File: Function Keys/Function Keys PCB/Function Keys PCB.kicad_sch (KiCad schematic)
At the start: 0 parts

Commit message: Added keys to schematic
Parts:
- added D? (x13): D_Small, symbol Device:D_Small
- added MX? (x13): MX-NoLED, symbol MX_Alps_Hybrid:MX-NoLED
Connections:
- new net: D?.2 (A), MX?.2 (ROW) (x13)
- new net COL0: MX?.1 (COL)
- new net COL1: MX?.1 (COL)
- new net COL10: MX?.1 (COL)
- new net COL11: MX?.1 (COL)
- new net COL12: MX?.1 (COL)
- new net COL2: MX?.1 (COL)
- new net COL3: MX?.1 (COL)
- new net COL4: MX?.1 (COL)
- new net COL5: MX?.1 (COL)
- new net COL6: MX?.1 (COL)
- new net COL7: MX?.1 (COL)
- new net COL8: MX?.1 (COL)
- new net COL9: MX?.1 (COL)
- new net ROW0: D?.1 (K), D?.1 (K), D?.1 (K), D?.1 (K), D?.1 (K), D?.1 (K), D?.1 (K), D?.1 (K), D?.1 (K), D?.1 (K), D?.1 (K), D?.1 (K), D?.1 (K)

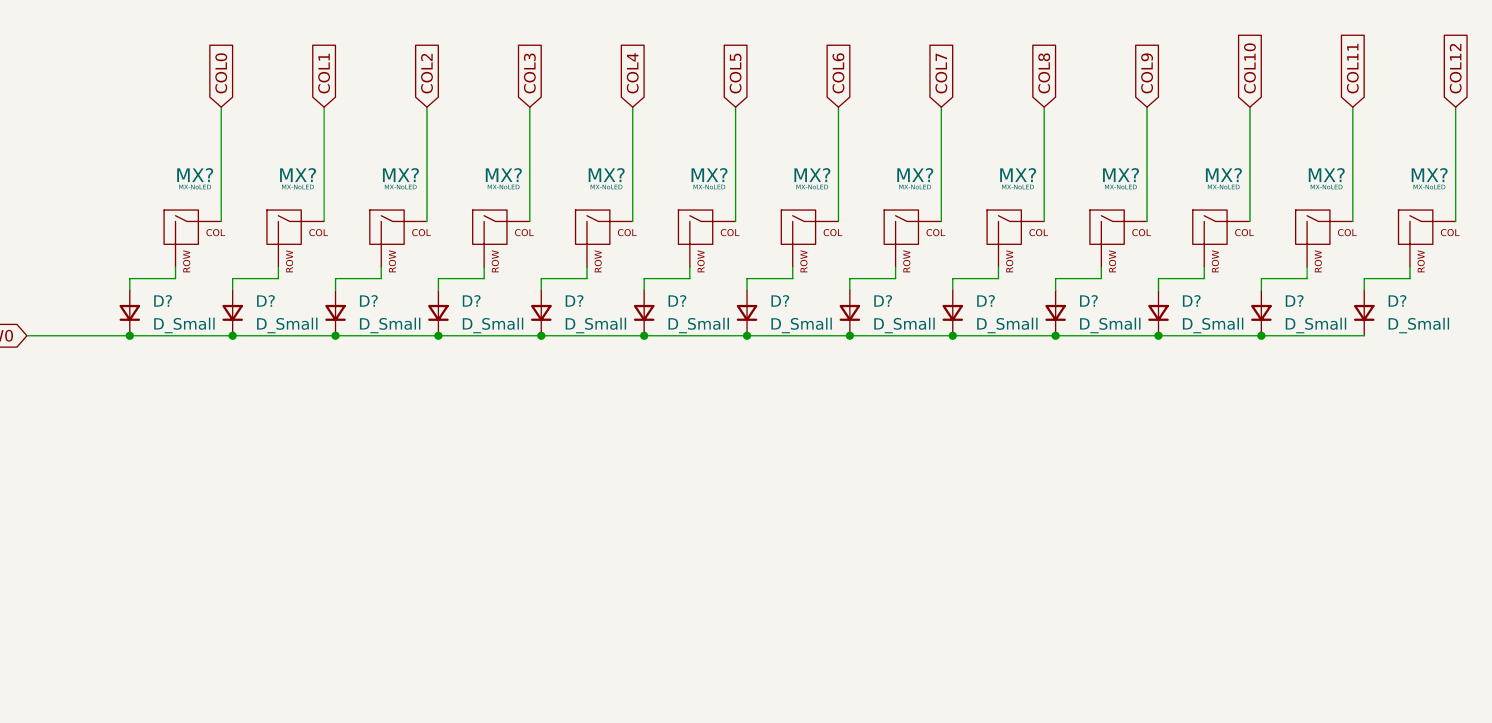
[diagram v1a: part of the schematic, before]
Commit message: Added connectors, labeled keys
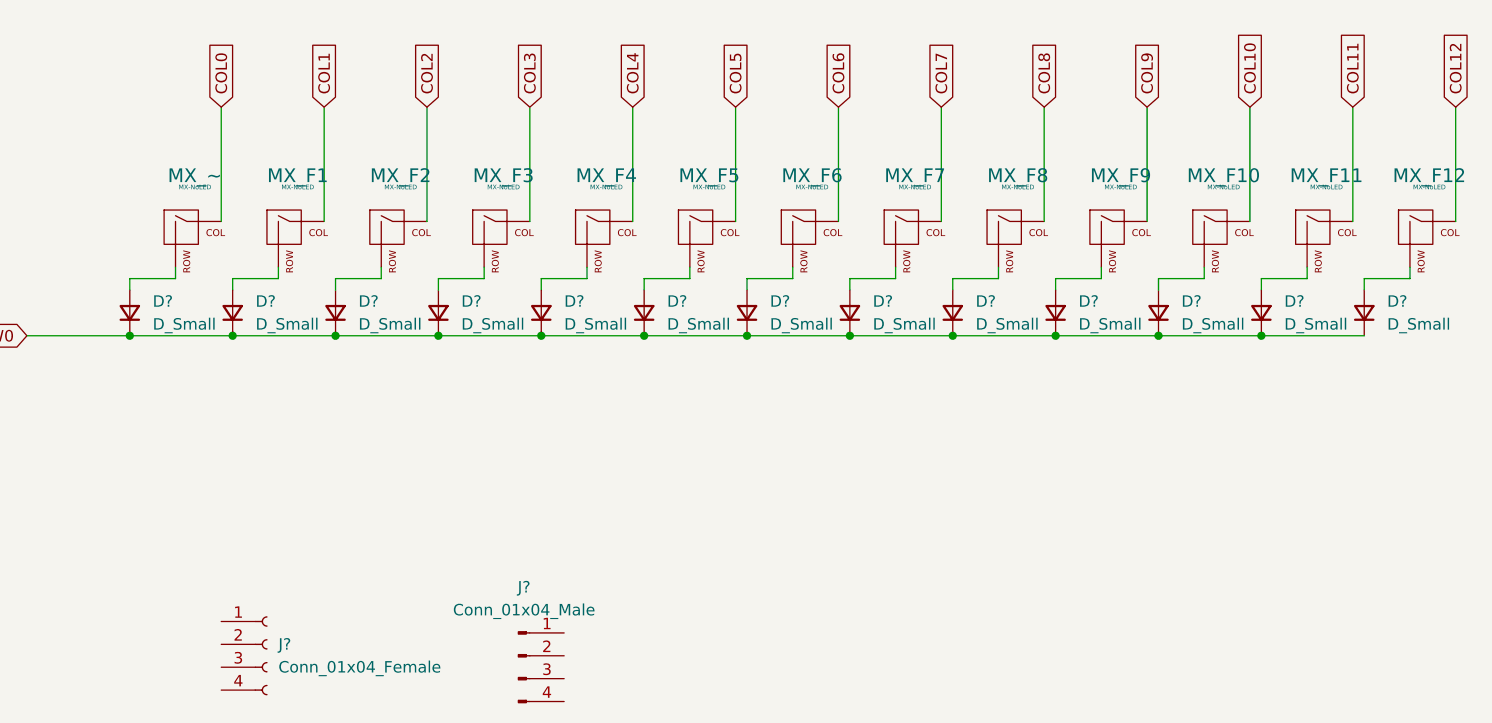
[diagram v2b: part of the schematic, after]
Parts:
- added J?: Conn_01x04_Male, symbol Connector:Conn_01x04_Male
- added J?: Conn_01x04_Female, symbol Connector:Conn_01x04_Female
- gave numbers to parts that had none: 13
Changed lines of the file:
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@@
   (symbol (lib_id "MX_Alps_Hybrid:MX-NoLED") (at 182.88 68.58 0) (unit 1)
     (in_bom yes) (on_board yes) (fields_autoplaced)
-    (property "Reference" "MX?" (id 0) (at 183.7656 62.23 0)
+    (property "Reference" "MX_F8" (id 0) (at 183.7656 62.23 0)
       (effects (font (size 1.524 1.524)))
     )
@@
   (symbol (lib_id "MX_Alps_Hybrid:MX-NoLED") (at 91.44 68.58 0) (unit 1)
     (in_bom yes) (on_board yes) (fields_autoplaced)
-    (property "Reference" "MX?" (id 0) (at 92.3256 62.23 0)
+    (property "Reference" "MX_~" (id 0) (at 92.3256 62.23 0)
       (effects (font (size 1.524 1.524)))
     )
@@
     (pin "2")
   )
+  (symbol (lib_id "Connector:Conn_01x04_Male") (at 128.27 115.57 0) (unit 1)
+    (in_bom yes) (on_board yes) (fields_autoplaced)
+    (property "Reference" "J?" (id 0) (at 128.905 107.95 0))
+    (property "Value" "Conn_01x04_Male" (id 1) (at 128.905 110.49 0))
+    (property "Footprint" "" (id 2) (at 128.27 115.57 0)
+      (effects (font (size 1.27 1.27)) hide)
+    )
+    (property "Datasheet" "~" (id 3) (at 128.27 115.57 0)
+      (effects (font (size 1.27 1.27)) hide)
+    )
+    (pin "1")
+    (pin "2")
+    (pin "3")
+    (pin "4")
+  )
+  (symbol (lib_id "Connector:Conn_01x04_Female") (at 100.33 114.3 0) (unit 1)
+    (in_bom yes) (on_board yes) (fields_autoplaced)
+    (property "Reference" "J?" (id 0) (at 101.6 114.2999 0)
+      (effects (font (size 1.27 1.27)) (justify left))
+    )
+    (property "Value" "Conn_01x04_Female" (id 1) (at 101.6 116.8399 0)
+      (effects (font (size 1.27 1.27)) (justify left))
+    )
+    (property "Footprint" "" (id 2) (at 100.33 114.3 0)
+      (effects (font (size 1.27 1.27)) hide)
+    )
+    (property "Datasheet" "~" (id 3) (at 100.33 114.3 0)
+      (effects (font (size 1.27 1.27)) hide)
+    )
+    (pin "1")
+    (pin "2")
+    (pin "3")
+    (pin "4")
+  )
   (symbol (lib_id "Device:D_Small") (at 222.25 77.47 90) (unit 1)
     (in_bom yes) (on_board yes) (fields_autoplaced)
@@
   (symbol (lib_id "MX_Alps_Hybrid:MX-NoLED") (at 160.02 68.58 0) (unit 1)
     (in_bom yes) (on_board yes) (fields_autoplaced)
-    (property "Reference" "MX?" (id 0) (at 160.9056 62.23 0)
+    (property "Reference" "MX_F6" (id 0) (at 160.9056 62.23 0)
       (effects (font (size 1.524 1.524)))
     )
@@
   (symbol (lib_id "MX_Alps_Hybrid:MX-NoLED") (at 205.74 68.58 0) (unit 1)
     (in_bom yes) (on_board yes) (fields_autoplaced)
-    (property "Reference" "MX?" (id 0) (at 206.6256 62.23 0)
+    (property "Reference" "MX_F10" (id 0) (at 206.6256 62.23 0)
       (effects (font (size 1.524 1.524)))
     )
@@
   (symbol (lib_id "MX_Alps_Hybrid:MX-NoLED") (at 148.59 68.58 0) (unit 1)
     (in_bom yes) (on_board yes) (fields_autoplaced)
-    (property "Reference" "MX?" (id 0) (at 149.4756 62.23 0)
+    (property "Reference" "MX_F5" (id 0) (at 149.4756 62.23 0)
       (effects (font (size 1.524 1.524)))
     )
@@
   (symbol (lib_id "MX_Alps_Hybrid:MX-NoLED") (at 114.3 68.58 0) (unit 1)
     (in_bom yes) (on_board yes) (fields_autoplaced)
-    (property "Reference" "MX?" (id 0) (at 115.1856 62.23 0)
+    (property "Reference" "MX_F2" (id 0) (at 115.1856 62.23 0)
       (effects (font (size 1.524 1.524)))
     )
@@
   (symbol (lib_id "MX_Alps_Hybrid:MX-NoLED") (at 194.31 68.58 0) (unit 1)
     (in_bom yes) (on_board yes) (fields_autoplaced)
-    (property "Reference" "MX?" (id 0) (at 195.1956 62.23 0)
+    (property "Reference" "MX_F9" (id 0) (at 195.1956 62.23 0)
       (effects (font (size 1.524 1.524)))
     )
@@
   (symbol (lib_id "MX_Alps_Hybrid:MX-NoLED") (at 171.45 68.58 0) (unit 1)
     (in_bom yes) (on_board yes) (fields_autoplaced)
-    (property "Reference" "MX?" (id 0) (at 172.3356 62.23 0)
+    (property "Reference" "MX_F7" (id 0) (at 172.3356 62.23 0)
       (effects (font (size 1.524 1.524)))
     )
@@
   (symbol (lib_id "MX_Alps_Hybrid:MX-NoLED") (at 125.73 68.58 0) (unit 1)
     (in_bom yes) (on_board yes) (fields_autoplaced)
-    (property "Reference" "MX?" (id 0) (at 126.6156 62.23 0)
+    (property "Reference" "MX_F3" (id 0) (at 126.6156 62.23 0)
       (effects (font (size 1.524 1.524)))
     )
@@
   (symbol (lib_id "MX_Alps_Hybrid:MX-NoLED") (at 217.17 68.58 0) (unit 1)
     (in_bom yes) (on_board yes) (fields_autoplaced)
-    (property "Reference" "MX?" (id 0) (at 218.0556 62.23 0)
+    (property "Reference" "MX_F11" (id 0) (at 218.0556 62.23 0)
       (effects (font (size 1.524 1.524)))
     )
@@
   (symbol (lib_id "MX_Alps_Hybrid:MX-NoLED") (at 102.87 68.58 0) (unit 1)
     (in_bom yes) (on_board yes) (fields_autoplaced)
-    (property "Reference" "MX?" (id 0) (at 103.7556 62.23 0)
+    (property "Reference" "MX_F1" (id 0) (at 103.7556 62.23 0)
       (effects (font (size 1.524 1.524)))
     )
@@
   (symbol (lib_id "MX_Alps_Hybrid:MX-NoLED") (at 228.6 68.58 0) (unit 1)
     (in_bom yes) (on_board yes) (fields_autoplaced)
-    (property "Reference" "MX?" (id 0) (at 229.4856 62.23 0)
+    (property "Reference" "MX_F12" (id 0) (at 229.4856 62.23 0)
       (effects (font (size 1.524 1.524)))
     )
@@
   (symbol (lib_id "MX_Alps_Hybrid:MX-NoLED") (at 137.16 68.58 0) (unit 1)
     (in_bom yes) (on_board yes) (fields_autoplaced)
-    (property "Reference" "MX?" (id 0) (at 138.0456 62.23 0)
+    (property "Reference" "MX_F4" (id 0) (at 138.0456 62.23 0)
       (effects (font (size 1.524 1.524)))
     )
@@
       (reference "D?") (unit 1) (value "D_Small") (footprint "")
     )
+    (path "/2bb70fb0-16f1-48a5-892c-a37f5f86e428"
+      (reference "J?") (unit 1) (value "Conn_01x04_Male") (footprint "")
+    )
+    (path "/2c079cf8-314d-4fe0-9a70-5d3272650d73"
+      (reference "J?") (unit 1) (value "Conn_01x04_Female") (footprint "")
+    )
+    (path "/953e6a73-9071-4c3b-9621-8aa02821bfc7"
+      (reference "MX_F1") (unit 1) (value "MX-NoLED") (footprint "")
+    )
+    (path "/5d46faef-5a1d-4fde-b7e9-a76b95fc2fec"
+      (reference "MX_F2") (unit 1) (value "MX-NoLED") (footprint "")
+    )
+    (path "/6e281010-a709-474f-8a51-f08f7114458d"
+      (reference "MX_F3") (unit 1) (value "MX-NoLED") (footprint "")
+    )
+    (path "/9dd67abb-a1b2-404e-9cf6-cff85d0f81d3"
+      (reference "MX_F4") (unit 1) (value "MX-NoLED") (footprint "")
+    )
+    (path "/50312df6-7b26-4b0a-afa6-b0ec2230735c"
+      (reference "MX_F5") (unit 1) (value "MX-NoLED") (footprint "")
+    )
+    (path "/433704dd-7939-4149-8b2e-1fb8d447ee43"
+      (reference "MX_F6") (unit 1) (value "MX-NoLED") (footprint "")
+    )
+    (path "/6d341050-f1dc-48f1-9b8d-80e5be0e410d"
+      (reference "MX_F7") (unit 1) (value "MX-NoLED") (footprint "")
+    )
     (path "/004b74d2-af25-4a97-8987-6d8a328283e3"
-      (reference "MX?") (unit 1) (value "MX-NoLED") (footprint "")
+      (reference "MX_F8") (unit 1) (value "MX-NoLED") (footprint "")
+    )
+    (path "/5ddcb211-f334-4231-9e36-52ad5d4d795f"
+      (reference "MX_F9") (unit 1) (value "MX-NoLED") (footprint "")
+    )
+    (path "/4e99f445-0400-4a6f-bb9d-def844852a81"
+      (reference "MX_F10") (unit 1) (value "MX-NoLED") (footprint "")
+    )
+    (path "/93413e48-12b3-4c2b-a7e0-d0a6fc3c6de6"
+      (reference "MX_F11") (unit 1) (value "MX-NoLED") (footprint "")
+    )
+    (path "/9733483c-3919-4675-b73d-10e31040629d"
+      (reference "MX_F12") (unit 1) (value "MX-NoLED") (footprint "")
     )
     (path "/027fa4f5-4265-4496-a2d3-69414343d100"
-      (reference "MX?") (unit 1) (value "MX-NoLED") (footprint "")
-    )
-    (path "/433704dd-7939-4149-8b2e-1fb8d447ee43"
-      (reference "MX?") (unit 1) (value "MX-NoLED") (footprint "")
-    )
-    (path "/4e99f445-0400-4a6f-bb9d-def844852a81"
-      (reference "MX?") (unit 1) (value "MX-NoLED") (footprint "")
-    )
-    (path "/50312df6-7b26-4b0a-afa6-b0ec2230735c"
-      (reference "MX?") (unit 1) (value "MX-NoLED") (footprint "")
-    )
-    (path "/5d46faef-5a1d-4fde-b7e9-a76b95fc2fec"
-      (reference "MX?") (unit 1) (value "MX-NoLED") (footprint "")
-    )
-    (path "/5ddcb211-f334-4231-9e36-52ad5d4d795f"
-      (reference "MX?") (unit 1) (value "MX-NoLED") (footprint "")
-    )
-    (path "/6d341050-f1dc-48f1-9b8d-80e5be0e410d"
-      (reference "MX?") (unit 1) (value "MX-NoLED") (footprint "")
-    )
-    (path "/6e281010-a709-474f-8a51-f08f7114458d"
-      (reference "MX?") (unit 1) (value "MX-NoLED") (footprint "")
-    )
-    (path "/93413e48-12b3-4c2b-a7e0-d0a6fc3c6de6"
-      (reference "MX?") (unit 1) (value "MX-NoLED") (footprint "")
-    )
-    (path "/953e6a73-9071-4c3b-9621-8aa02821bfc7"
-      (reference "MX?") (unit 1) (value "MX-NoLED") (footprint "")
-    )
-    (path "/9733483c-3919-4675-b73d-10e31040629d"
-      (reference "MX?") (unit 1) (value "MX-NoLED") (footprint "")
-    )
-    (path "/9dd67abb-a1b2-404e-9cf6-cff85d0f81d3"
-      (reference "MX?") (unit 1) (value "MX-NoLED") (footprint "")
-    )
-  )
+      (reference "MX_~") (unit 1) (value "MX-NoLED") (footprint "")
+    )
+  )

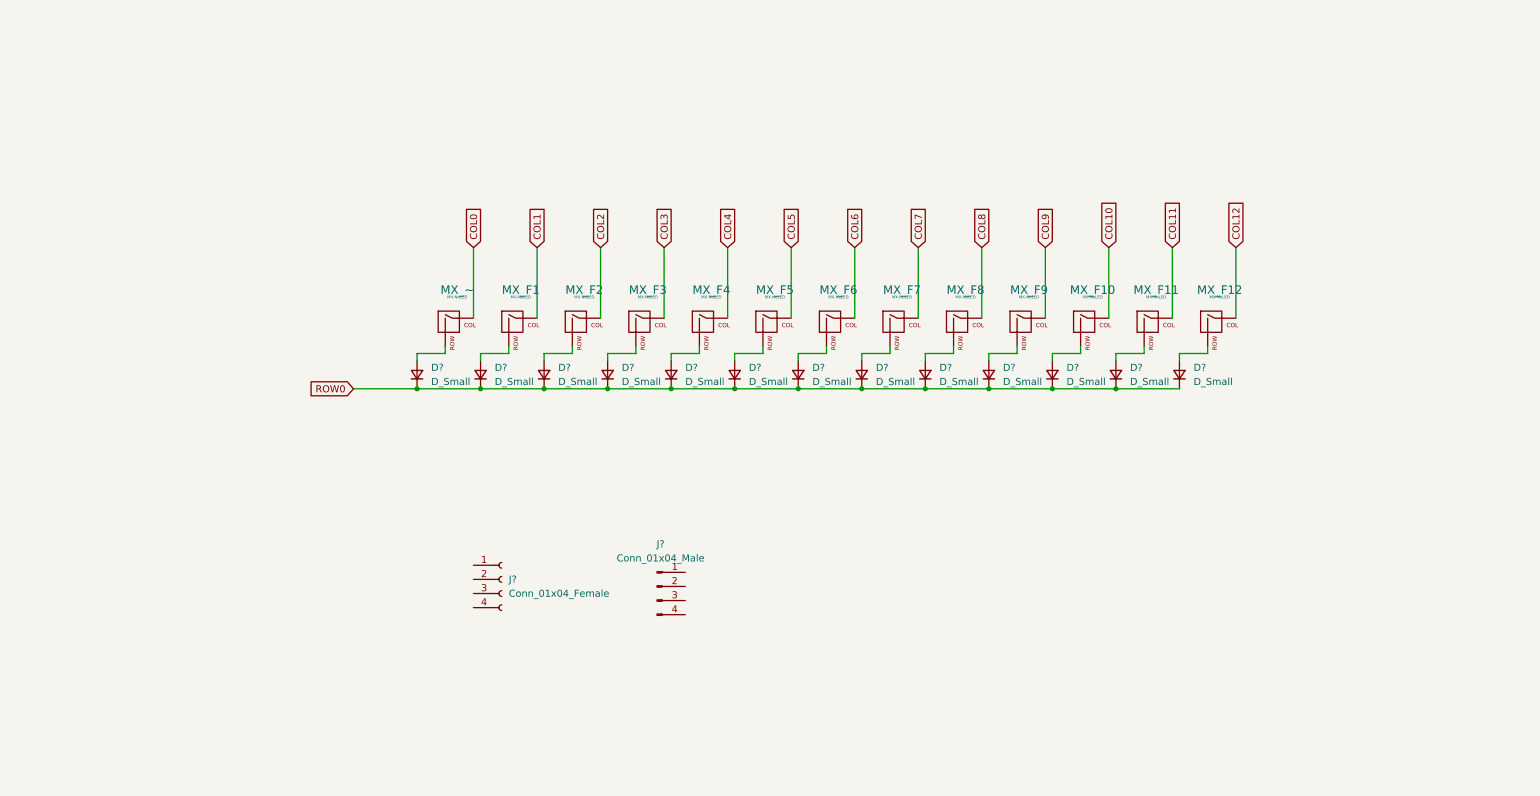
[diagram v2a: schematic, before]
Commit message: Added connectors, assigned footprints
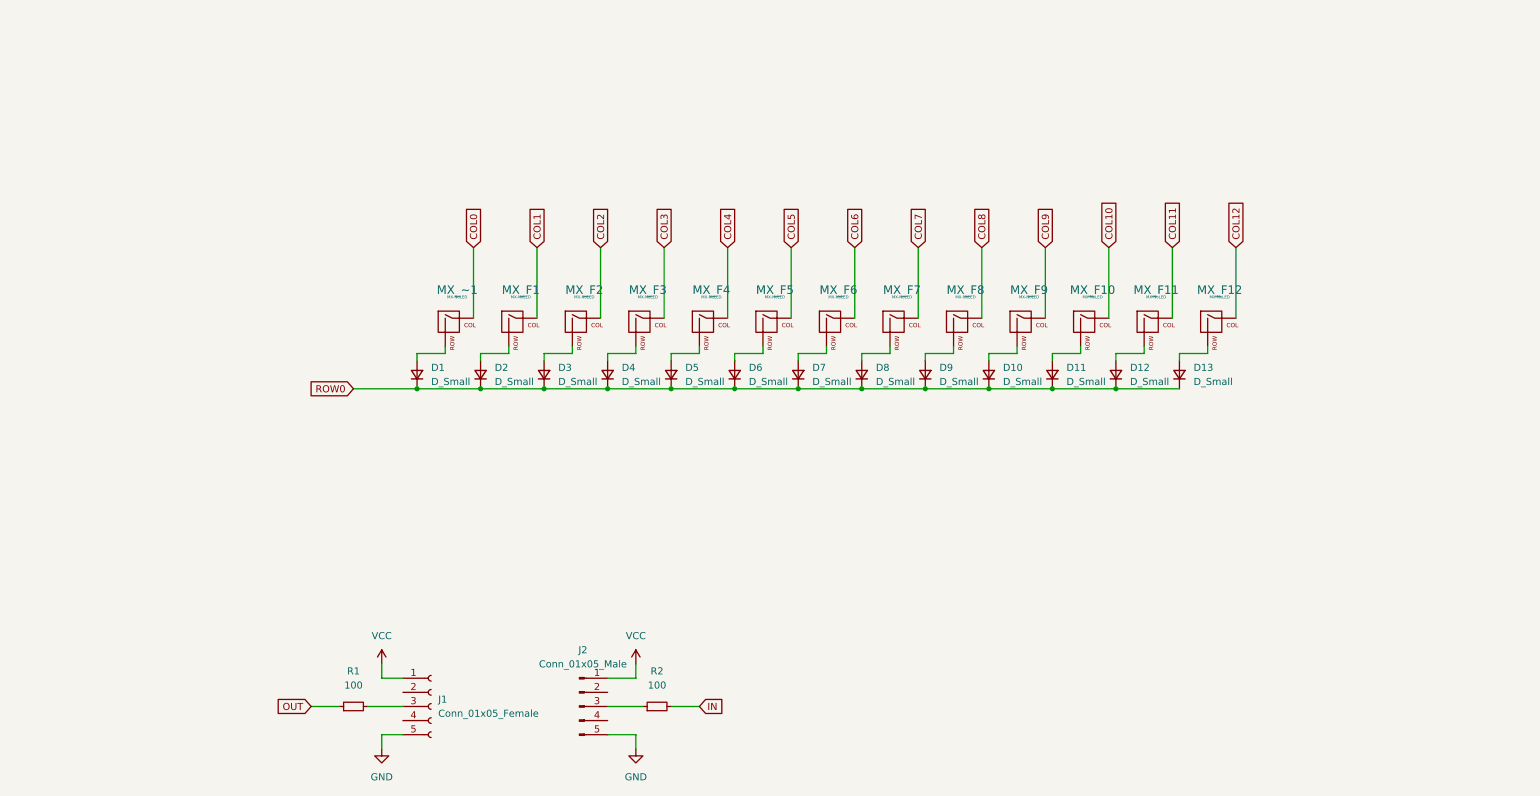
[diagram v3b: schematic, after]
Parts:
- removed J?: Conn_01x04_Male, symbol Connector:Conn_01x04_Male
- removed J?: Conn_01x04_Female, symbol Connector:Conn_01x04_Female
- added J1: Conn_01x05_Female, Connector_JST:JST_PH_B5B-PH-K_1x05_P2.00mm_Vertical, symbol Connector:Conn_01x05_Female
- added J2: Conn_01x05_Male, Connector_JST:JST_PH_B5B-PH-K_1x05_P2.00mm_Vertical, symbol Connector:Conn_01x05_Male
- added R1, R2: 100, Resistor_SMD:R_0805_2012Metric, symbol Device:R_Small
- D1, D10, D11, D12, D13, D2, D3, D4, D5, D6, D7, D8, D9: renamed from D?; footprint (none) -> Diode_SMD:D_SOD-123
- MX_F1, MX_F10, MX_F11, MX_F12, MX_F2, MX_F3, MX_F4, MX_F5, MX_F6, MX_F7, MX_F8, MX_F9: footprint (none) -> MX_Alps_Hybrid:MX-1U-NoLED
- MX_~1: renamed from MX_~; footprint (none) -> MX_Alps_Hybrid:MX-1U-NoLED
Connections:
- new net: J2.3 (Pin_3), R2.1
- new net: J1.3 (Pin_3), R1.2
- new net GND: J1.5 (Pin_5), J2.5 (Pin_5)
- new net IN: R2.2
- new net OUT: R1.1
- new net VCC: J1.1 (Pin_1), J2.1 (Pin_1)
